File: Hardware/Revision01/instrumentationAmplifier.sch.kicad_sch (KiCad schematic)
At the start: 8 parts, among them U6 TLV9062IDSGR

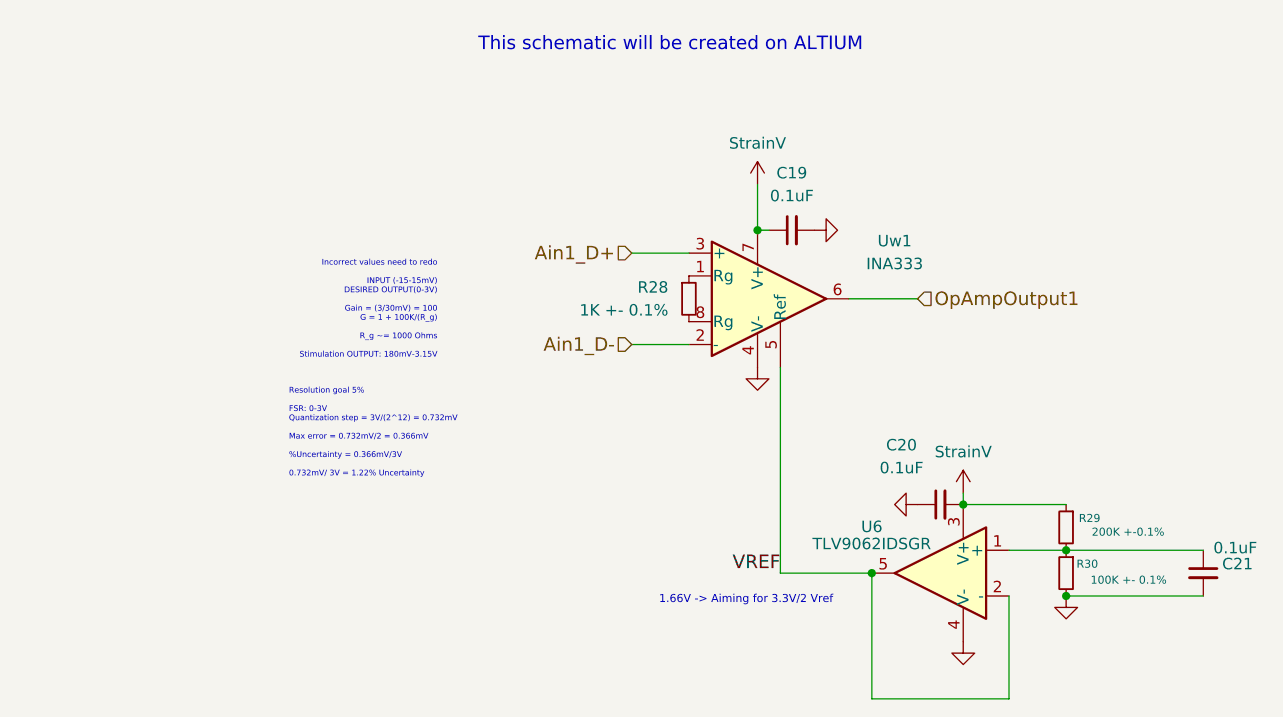
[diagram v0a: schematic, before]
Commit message: Schematic small details, and beginning wiring
Placed capacitors( in correct polarity)
Branch fuses should be put on the branches(sensor Amplifiers) - as they protect branches
Added Main fuse(protecting main circuit - from connector)
Changed all component sizes back to 0805 atleast
Started PCB WIRING
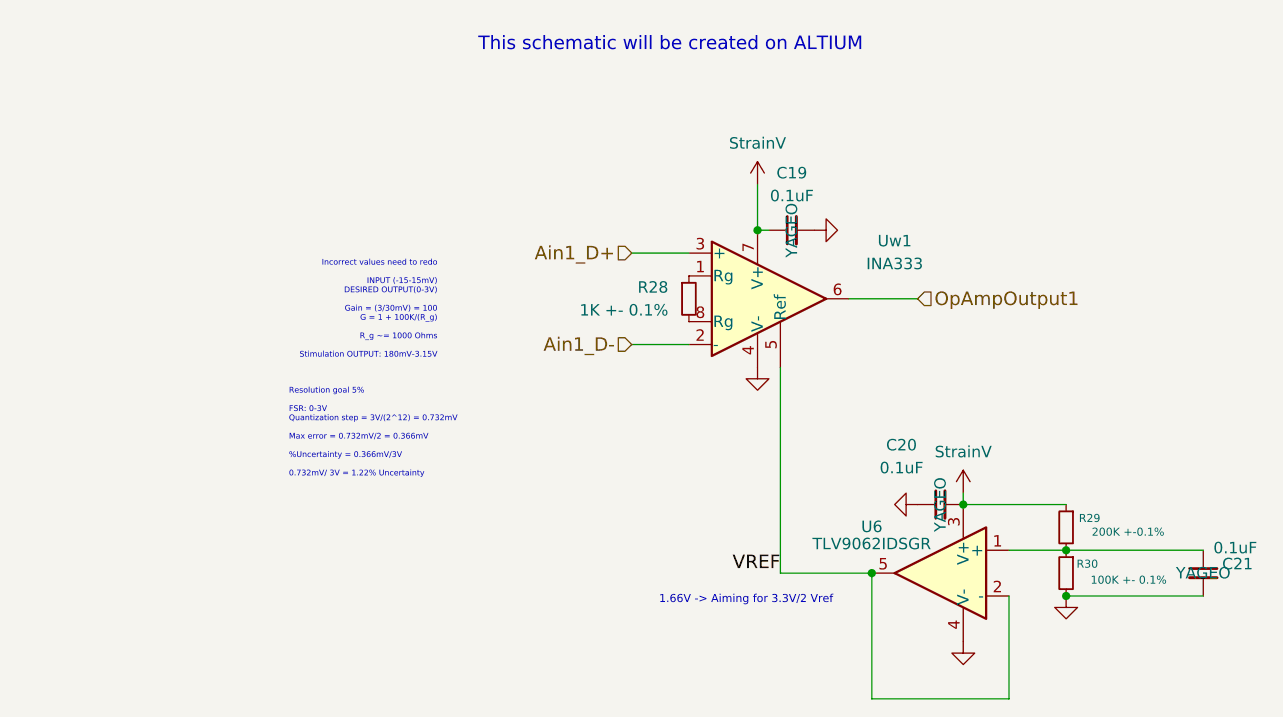
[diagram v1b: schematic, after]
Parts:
- C19, C20, C21: Manufacturer (none) -> YAGEO
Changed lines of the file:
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@@
+			)
+		)
+		(property "Manufacturer" "YAGEO"
+			(at 186.69 115.57 0)
+			(effects
+				(font
+					(size 1.27 1.27)
+				)
 			)
 		)
@@
 			)
 		)
+		(property "Manufacturer" "YAGEO"
+			(at 140.97 77.47 0)
+			(effects
+				(font
+					(size 1.27 1.27)
+				)
+			)
+		)
 		(pin "2"
 		)
@@
 			)
 		)
+		(property "Manufacturer" "YAGEO"
+			(at 157.48 107.95 0)
+			(effects
+				(font
+					(size 1.27 1.27)
+				)
+			)
+		)

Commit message: part B schematic complete:
- fuse added
- input terminals protected against S.C
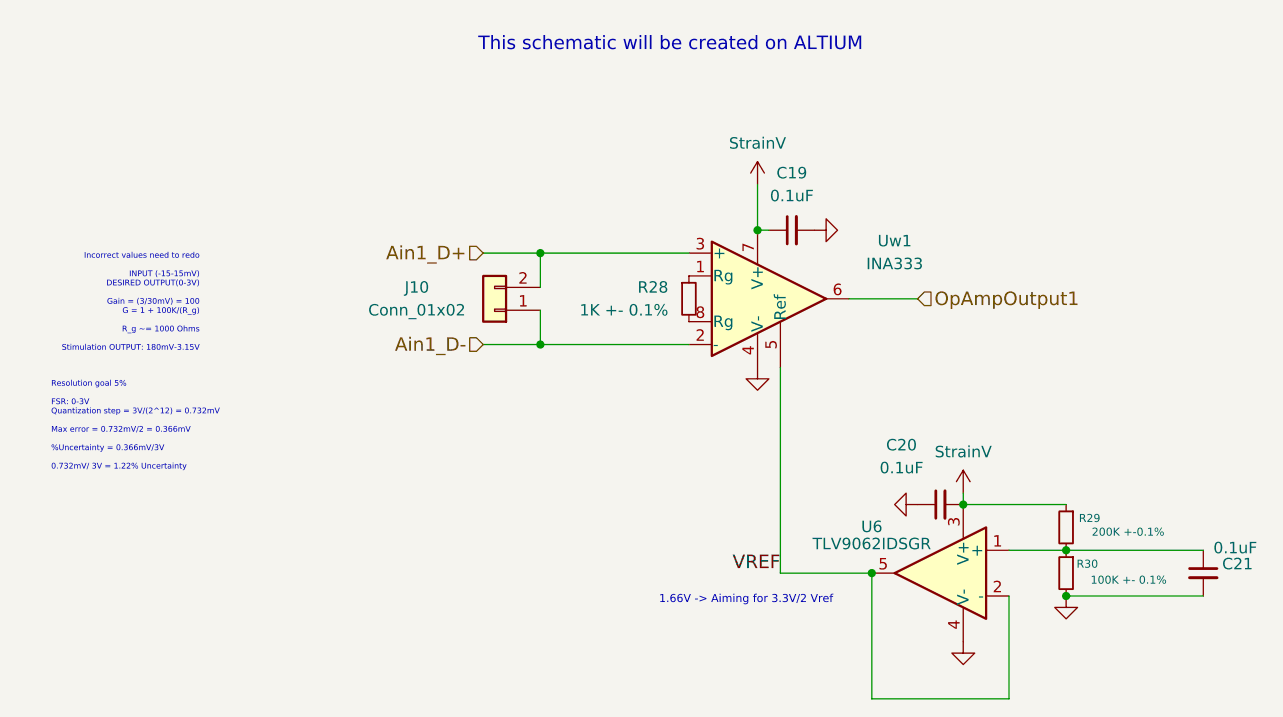
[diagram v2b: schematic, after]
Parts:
- added J10: Conn_01x02, symbol Connector_Generic:Conn_01x02
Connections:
- net Ain1_D+: now also J10.2 (Pin_2)
- net Ain1_D-: now also J10.1 (Pin_1)
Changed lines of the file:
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@@
 	(text "Resolution goal 5%\n\nFSR: 0-3V\nQuantization step = 3V/(2^12) = 0.732mV\n\nMax error = 0.732mV/2 = 0.366mV\n\n%Uncertainty = 0.366mV/3V\n\n0.732mV/ 3V = 1.22% Uncertainty\n\n\n\n"
 		(exclude_from_sim no)
-		(at 85.09 101.6 0)
+		(at 58.674 100.838 0)
 		(effects
 			(font
@@
 	(text "Incorrect values need to redo\n\nINPUT (-15-15mV) \nDESIRED OUTPUT(0-3V)\n\nGain = (3/30mV) = 100\nG = 1 + 100K/(R_g)\n\nR_g ~= 1000 Ohms\n\nStimulation OUTPUT: 180mV-3.15V"
 		(exclude_from_sim no)
-		(at 101.6 86.36 0)
+		(at 75.184 85.598 0)
 		(effects
 			(font
@@
 	)
 	(junction
+		(at 113.03 80.01)
+		(diameter 0)
+		(color 0 0 0 0)
+	)
+	(junction
 		(at 160.02 107.95)
 		(diameter 0)
@@
 	)
 	(junction
+		(at 113.03 90.17)
+		(diameter 0)
+		(color 0 0 0 0)
+	)
+	(junction
 		(at 171.45 118.11)
 		(diameter 0)
@@
 	(wire
 		(pts
+			(xy 113.03 90.17) (xy 113.03 86.36)
+		)
+		(stroke
+			(width 0)
+			(type default)
+		)
+	)
+	(wire
+		(pts
 			(xy 147.32 85.09) (xy 154.94 85.09)
 		)
@@
 	(wire
 		(pts
+			(xy 113.03 80.01) (xy 129.54 80.01)
+		)
+		(stroke
+			(width 0)
+			(type default)
+		)
+	)
+	(wire
+		(pts
 			(xy 165.1 129.54) (xy 149.86 129.54)
 		)
@@
 	(wire
 		(pts
-			(xy 123.19 90.17) (xy 129.54 90.17)
+			(xy 113.03 83.82) (xy 113.03 80.01)
+		)
+		(stroke
+			(width 0)
+			(type default)
+		)
+	)
+	(wire
+		(pts
+			(xy 106.68 90.17) (xy 113.03 90.17)
 		)
 		(stroke
@@
 	(wire
 		(pts
-			(xy 123.19 80.01) (xy 129.54 80.01)
+			(xy 106.68 80.01) (xy 113.03 80.01)
 		)
 		(stroke
@@
 		(pts
 			(xy 138.43 77.47) (xy 137.16 77.47)
+		)
+		(stroke
+			(width 0)
+			(type default)
+		)
+	)
+	(wire
+		(pts
+			(xy 129.54 90.17) (xy 113.03 90.17)
 		)
 		(stroke
@@
 	(hierarchical_label "Ain1_D-"
 		(shape input)
-		(at 123.19 90.17 180)
+		(at 106.68 90.17 180)
 		(effects
 			(font
@@
 	(hierarchical_label "Ain1_D+"
 		(shape input)
-		(at 123.19 80.01 180)
+		(at 106.68 80.01 180)
 		(effects
 			(font
@@
 					(size 1.27 1.27)
 				)
+				(hide yes)
 			)
 		)
@@
 				(path "/955cc99e-a129-42cf-abc7-aa99813fdb5f/00000000-0000-0000-0000-00005eb1de63/14eb51a3-67a8-4f4f-b7c1-d030be0d073f"
 					(reference "C21")
+					(unit 1)
+				)
+			)
+		)
+	)
+	(symbol
+		(lib_id "Connector_Generic:Conn_01x02")
+		(at 107.95 86.36 180)
+		(unit 1)
+		(exclude_from_sim no)
+		(in_bom yes)
+		(on_board yes)
+		(dnp no)
+		(property "Reference" "J10"
+			(at 99.314 83.82 0)
+			(effects
+				(font
+					(size 1.27 1.27)
+				)
+			)
+		)
+		(property "Value" "Conn_01x02"
+			(at 99.314 86.36 0)
+			(effects
+				(font
+					(size 1.27 1.27)
+				)
+			)
+		)
+		(property "Footprint" ""
+			(at 107.95 86.36 0)
+			(effects
+				(font
+					(size 1.27 1.27)
+				)
+				(hide yes)
+			)
+		)
+		(property "Datasheet" "~"
+			(at 107.95 86.36 0)
+			(effects
+				(font
+					(size 1.27 1.27)
+				)
+				(hide yes)
+			)
+		)
+		(property "Description" "Generic connector, single row, 01x02, script generated (kicad-library-utils/schlib/autogen/connector/)"
+			(at 107.95 86.36 0)
+			(effects
+				(font
+					(size 1.27 1.27)
+				)
+				(hide yes)
+			)
+		)
+		(pin "1"
+		)
+		(pin "2"
+		)
+		(instances
+			(project ""
+				(path "/955cc99e-a129-42cf-abc7-aa99813fdb5f/00000000-0000-0000-0000-00005eb1de63/14eb51a3-67a8-4f4f-b7c1-d030be0d073f"
+					(reference "J10")
 					(unit 1)
 				)
@@
 					(size 1.27 1.27)
 				)
+				(hide yes)
 			)
 		)
@@
 					(size 1.27 1.27)
 				)
-			)
-		)
+				(hide yes)
+			)
+		)

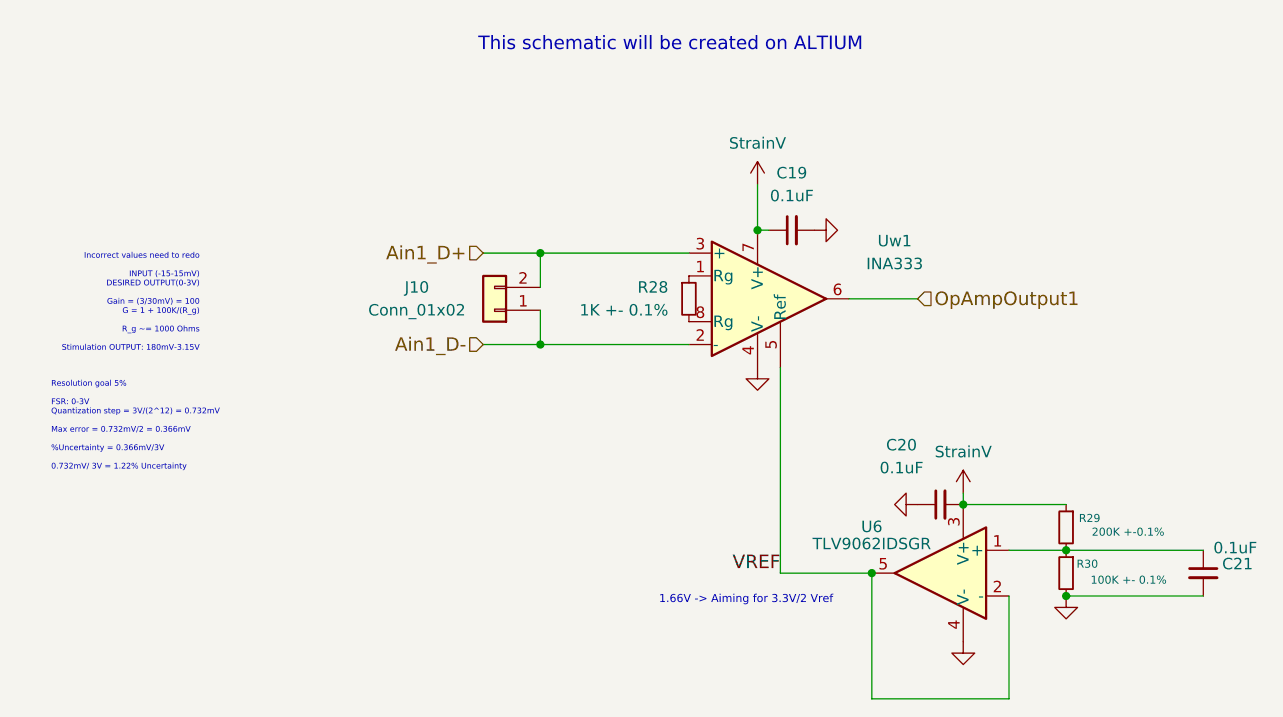
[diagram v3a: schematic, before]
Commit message: Schematic changes  - Remove LDO  - find new battery holder  - repicked power switch  - voltage divider value changed R2=5K  - branch fuses moved back to main to ensure wires stay downstream
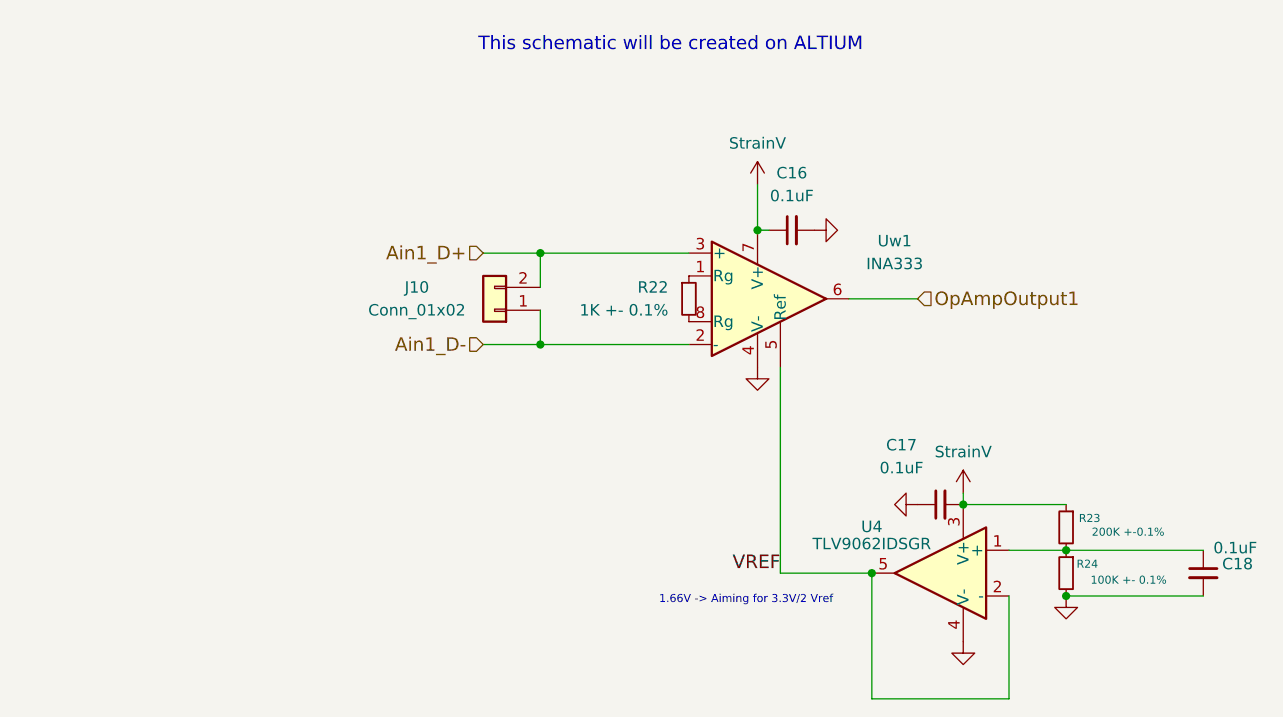
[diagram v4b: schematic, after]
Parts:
- renumbered C19 to C16, C20 to C17, C21 to C18, R28 to R22, R29 to R23, R30 to R24, U6 to U4
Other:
- note removed: "Incorrect values need to redo INPUT (-15-15mV) DESIRED OUTPUT(0-3V) Gain = (3/30mV) = 100 G = 1 + 100K/(R_g) R_g ~= 1000 Ohms Stimulation OUTPUT: 180mV-3.15V"
- note removed: "Resolution goal 5% FSR: 0-3V Quantization step = 3V/(2^12) = 0.732mV Max error = 0.732mV/2 = 0.366mV %Uncertainty = 0.366mV/3V 0.732mV/ 3V = 1.22% Uncertainty"

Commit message: rewired and re-routed traces on strainAmplifier
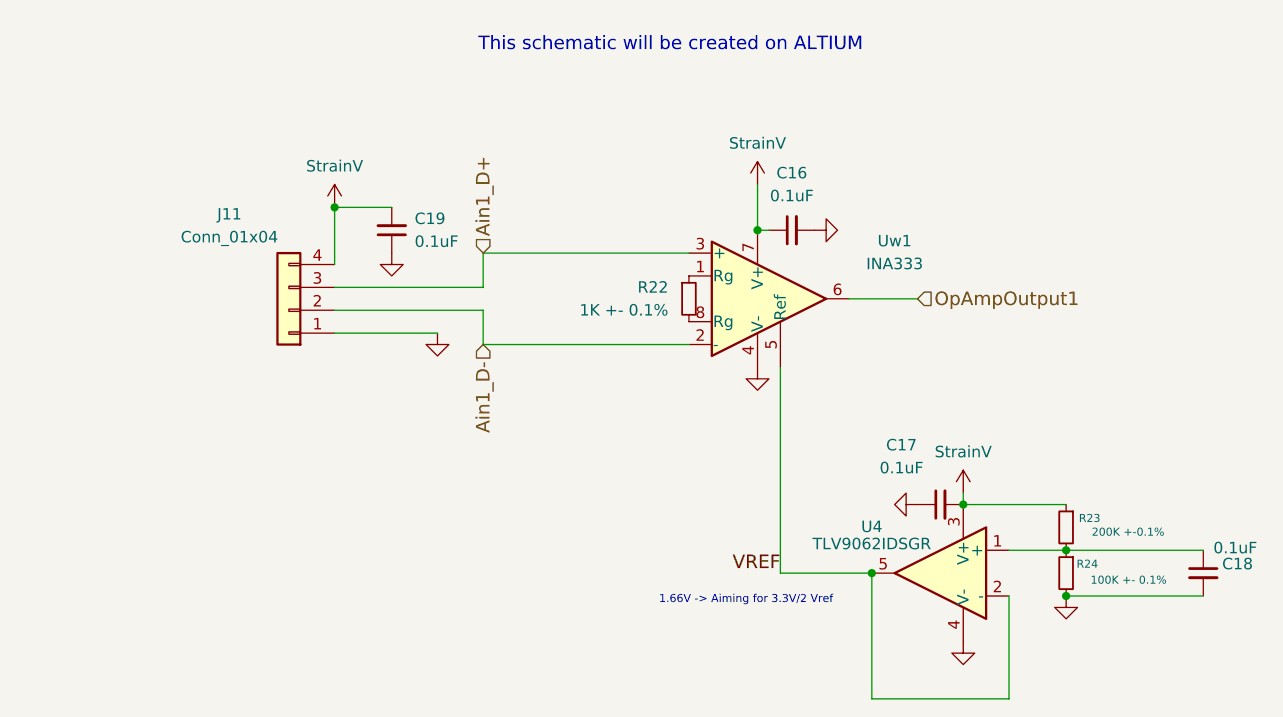
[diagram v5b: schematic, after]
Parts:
- removed J10: Conn_01x02, symbol Connector_Generic:Conn_01x02
- added C19: 0.1uF, Capacitor_SMD:C_0805_2012Metric_Pad1.18x1.45mm_HandSolder, symbol Device:C_Small
- added J11: Conn_01x04, symbol Connector_Generic:Conn_01x04
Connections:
- net Ain1_D+: now also J11.3 (Pin_3)
- net Ain1_D-: now also J11.2 (Pin_2)
- net GND: now also C19.1, J11.1 (Pin_1)
- new net: C19.2, J11.4 (Pin_4)
